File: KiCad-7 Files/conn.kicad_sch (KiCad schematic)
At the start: 6 parts, among them J1 2383942-4, J2 Molex 0955406888

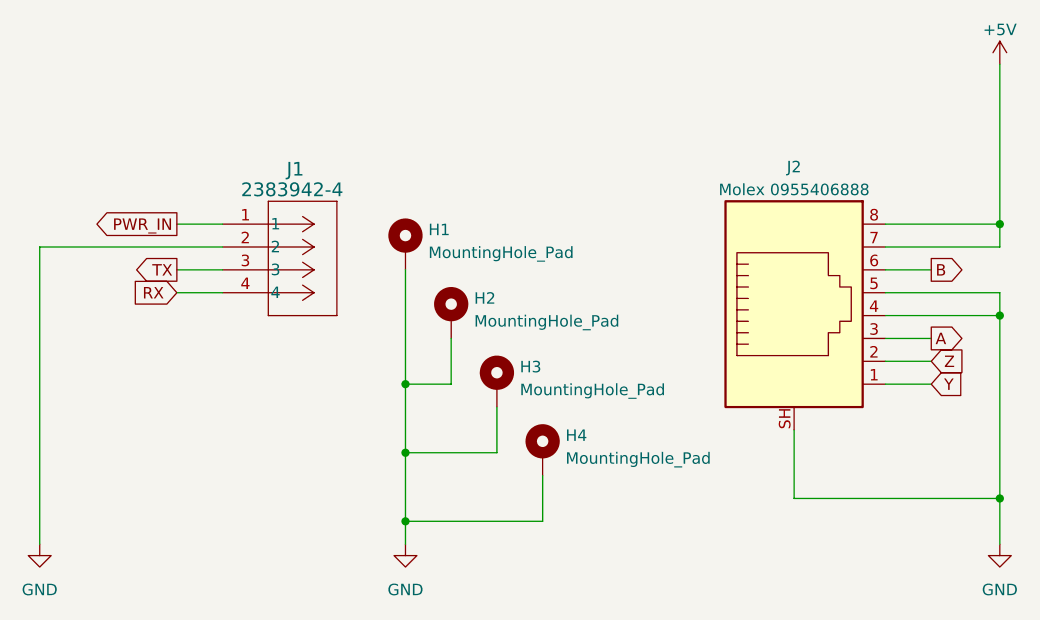
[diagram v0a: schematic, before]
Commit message: Add files via upload
upload new kicad 7 files with certification mark
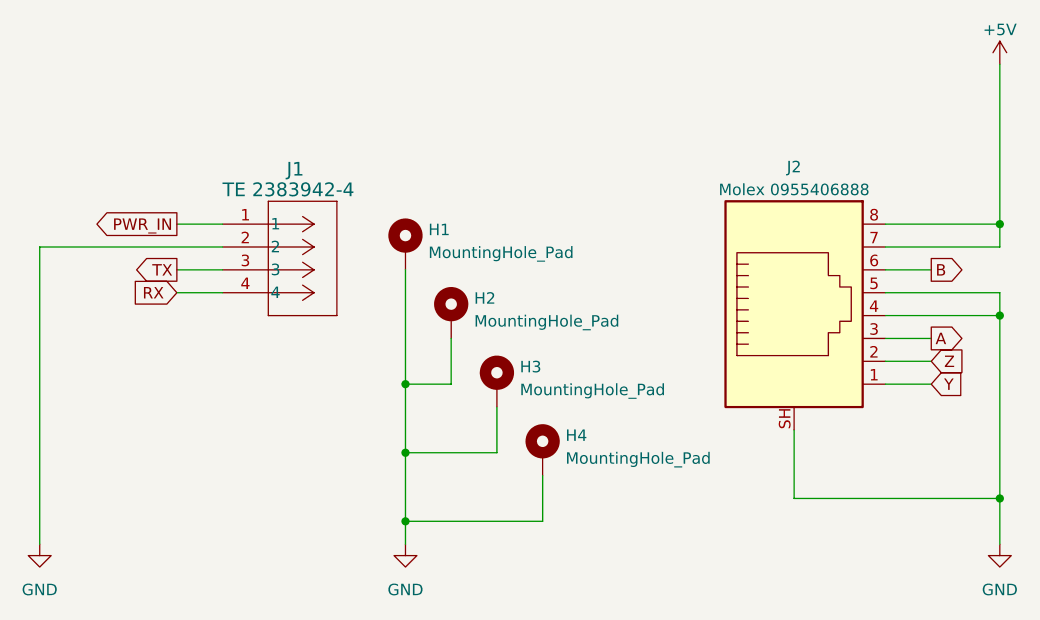
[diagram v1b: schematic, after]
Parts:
- J1: value 2383942-4 -> TE 2383942-4
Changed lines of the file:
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@@
       (effects (font (size 1.524 1.524)) (justify left))
     )
-    (property "Value" "2383942-4" (at 106.172 74.93 0)
+    (property "Value" "TE 2383942-4" (at 104.14 74.93 0)
       (effects (font (size 1.524 1.524)) (justify left))
     )
